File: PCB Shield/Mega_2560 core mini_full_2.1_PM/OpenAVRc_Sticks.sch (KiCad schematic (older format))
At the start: 57 parts, among them P11 Trim, P12 Stick_left, P13 Stick_right, P14 Switch, P23 Rot_1, P24 Rot_2, P25 Keys, P28 5v/3,3v manches, P31 Pot2, P32 Pot1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

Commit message: Update pcb files v2.1
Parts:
- added P33: 5V_CODERS, symbol CONN_01X02
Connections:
- net VCC: now also P33.1 (P1), P33.2 (P2)

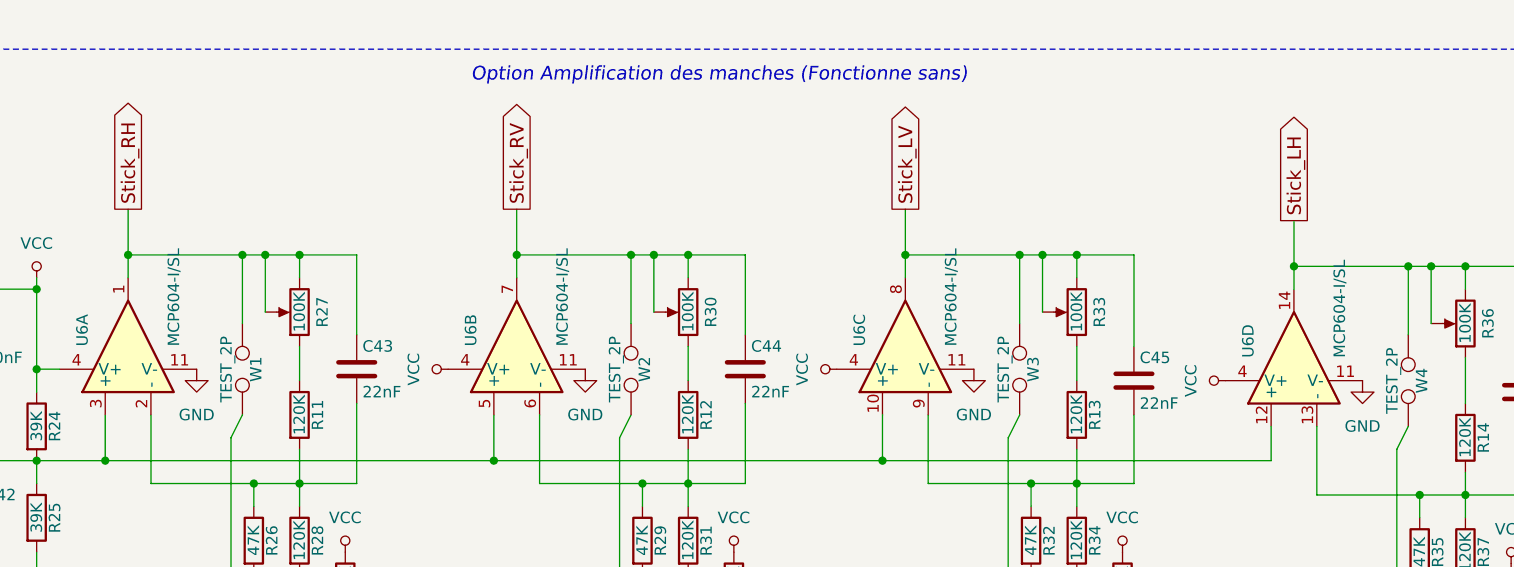
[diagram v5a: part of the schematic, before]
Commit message: Update shematic & PCB files
- replace mcp604 by a mcp6004.
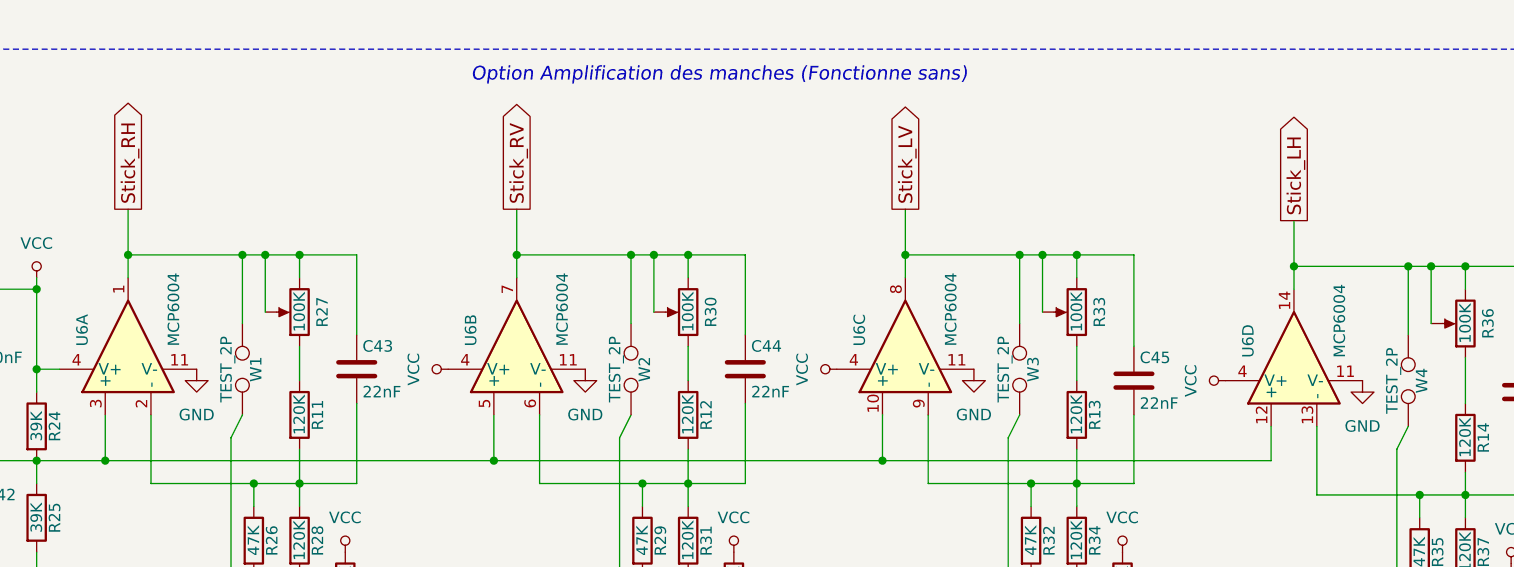
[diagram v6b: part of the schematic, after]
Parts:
- U6: value MCP604-I/SL -> MCP6004
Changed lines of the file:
@@
 P 6100 4500
 F 0 "U6" H 6100 4700 50  0000 L CNN
-F 1 "MCP604-I/SL" H 6100 4300 50  0000 L CNN
+F 1 "MCP6004" H 6100 4300 50  0000 L CNN
 F 2 "Librairie master:SOP14" H 6050 4600 50  0001 C CNN
 F 3 "" H 6150 4700 50  0000 C CNN
@@
 P 9500 4550
 F 0 "U6" H 9500 4750 50  0000 L CNN
-F 1 "MCP604-I/SL" H 9500 4350 50  0000 L CNN
+F 1 "MCP6004" H 9500 4350 50  0000 L CNN
 F 2 "Librairie master:SOP14" H 9450 4650 50  0001 C CNN
 F 3 "" H 9550 4750 50  0000 C CNN
@@
 P 7800 4500
 F 0 "U6" H 7800 4700 50  0000 L CNN
-F 1 "MCP604-I/SL" H 7800 4300 50  0000 L CNN
+F 1 "MCP6004" H 7800 4300 50  0000 L CNN
 F 2 "Librairie master:SOP14" H 7750 4600 50  0001 C CNN
 F 3 "" H 7850 4700 50  0000 C CNN
@@
 P 4400 4500
 F 0 "U6" H 4400 4700 50  0000 L CNN
-F 1 "MCP604-I/SL" H 4400 4300 50  0000 L CNN
+F 1 "MCP6004" H 4400 4300 50  0000 L CNN
 F 2 "Librairie master:SOP14" H 4350 4600 50  0001 C CNN
 F 3 "" H 4450 4700 50  0000 C CNN

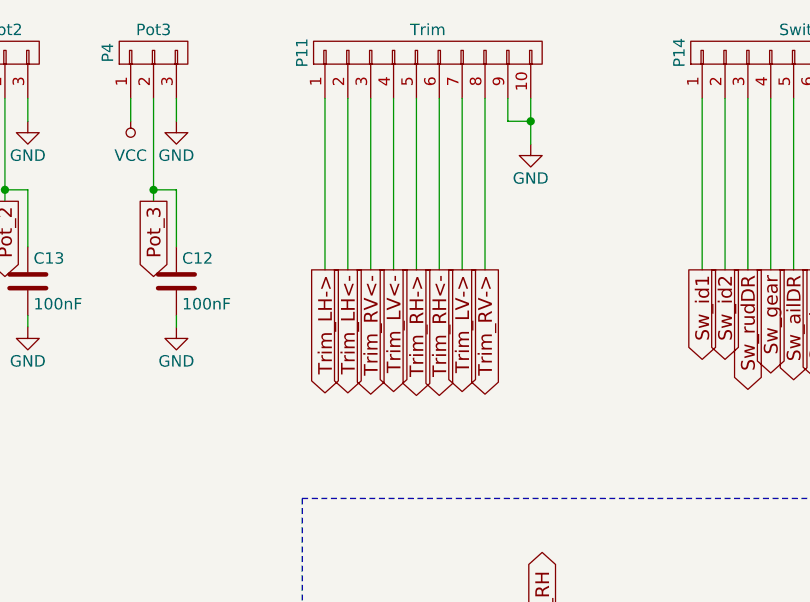
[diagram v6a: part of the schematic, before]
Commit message: Update schematic & pcb files
- change P11 pin out.
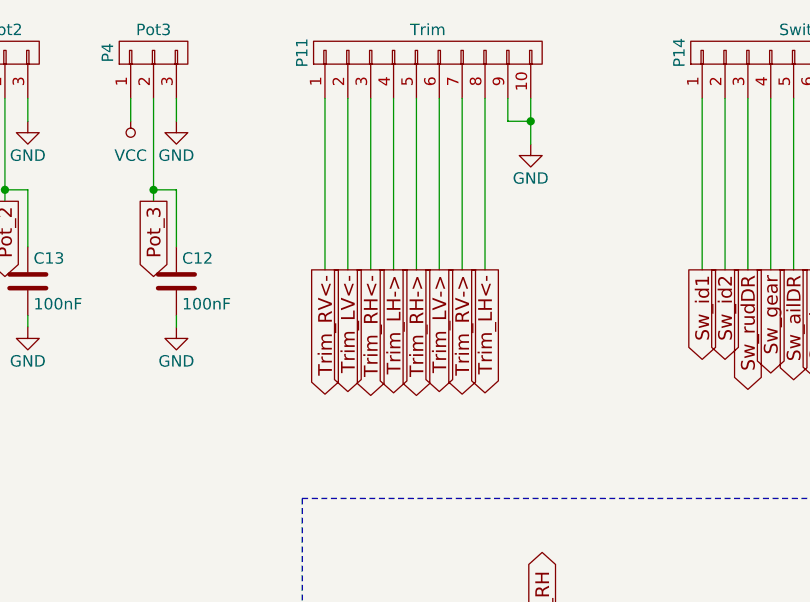
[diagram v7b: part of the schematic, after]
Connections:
- net Trim_LH->: now also P11.4 (P4); no longer P11.1 (P1)
- net Trim_LH<-: now also P11.8 (P8); no longer P11.2 (P2)
- net Trim_LV->: now also P11.6 (P6); no longer P11.7 (P7)
- net Trim_LV<-: now also P11.2 (P2); no longer P11.4 (P4)
- net Trim_RH<-: now also P11.3 (P3); no longer P11.6 (P6)
- net Trim_RV->: now also P11.7 (P7); no longer P11.8 (P8)
- net Trim_RV<-: now also P11.1 (P1); no longer P11.3 (P3)
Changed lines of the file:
@@
 Sheet 2 7
 Title "Shield Mega2560 core Full"
-Date "2018-02-15"
+Date "2018-02-21"
 Rev "2.10"
 Comp "© Team OpenAVRc"
@@
 $EndComp
 Wire Wire Line
+	3750 2200 3750 1450
+Wire Wire Line
+	4150 1450 4150 2200
+Wire Wire Line
 	3450 2200 3450 1450
 Wire Wire Line
-	3550 1450 3550 2200
+	3550 2200 3550 1450
+Wire Wire Line
+	3850 2200 3850 1450
 Wire Wire Line
 	3650 2200 3650 1450
 Wire Wire Line
-	3750 2200 3750 1450
-Wire Wire Line
-	3850 2200 3850 1450
-Wire Wire Line
 	3950 2200 3950 1450
 Wire Wire Line
 	4050 2200 4050 1450
-Wire Wire Line
-	4150 2200 4150 1450
 Wire Wire Line
 	4350 1450 4350 1650
@@
 Wire Wire Line
 	10000 2050 10000 1450
+Text GLabel 3750 2200 3    60   Output ~ 0
+Trim_LH->
+Text GLabel 4150 2200 3    60   Output ~ 0
+Trim_LH<-
 Text GLabel 3450 2200 3    60   Output ~ 0
-Trim_LH->
+Trim_RV<-
 Text GLabel 3550 2200 3    60   Output ~ 0
-Trim_LH<-
-Text GLabel 3650 2200 3    60   Output ~ 0
-Trim_RV<-
-Text GLabel 3750 2200 3    60   Output ~ 0
 Trim_LV<-
 Text GLabel 3850 2200 3    60   Output ~ 0
 Trim_RH->
+Text GLabel 3650 2200 3    60   Output ~ 0
+Trim_RH<-
 Text GLabel 3950 2200 3    60   Output ~ 0
-Trim_RH<-
+Trim_LV->
 Text GLabel 4050 2200 3    60   Output ~ 0
-Trim_LV->
-Text GLabel 4150 2200 3    60   Output ~ 0
 Trim_RV->
 Text GLabel 5100 2200 3    60   Output ~ 0
